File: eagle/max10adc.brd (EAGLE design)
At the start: 98 x 62 mm, 162 parts, among them IC1 MAX19506, IC2 MAX19506, J1 MOLEX_BNC_73100-0105, J2 MOLEX_BNC_73100-0105, J3 MOLEX_BNC_73100-0105, J4 MOLEX_BNC_73100-0105, K1 AQY21SOP, K2 AQY21SOP, K3 AQY21SOP, K4 AQY21SOP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

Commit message: 8.6 improvements
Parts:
- removed PIN_ANALOG, PIN_EXP_IO_1, PIN_EXP_IO_2, PIN_IO_2, PIN_PWRGND_AIN: MF-CON-2.54mm-01x08, Seeed-Connector -2016:H8-2.54
- added K5, K6, K7, K8: AQY21SOP, relay:SOP04
- added LED6, LED7, LED8: MF-LED-0805-RED, led:SML0805
- added PIN_AIN_IO2_PWRGND, PIN_ANALOG_IOEXP: 15-91-2160, pinhead+:2X08_SMT
- added RIN1_10K, RIN2_10K, RIN3_10K, RIN4_10K: 10K, resistor:R0805
- added RLED6, RLED7, RLED8: 560, resistor:R0805
- moved LED5 55.6 mm to (7.80, 1.00)
- moved RLED5 48.0 mm to (4.50, -0.40)
- moved R_SDA 20.2 mm to (-2.60, 23.6)
- moved R_SCL 19.9 mm to (2.90, 23.6)
- moved IOEXPAND_0X20_BOT 19.1 mm to (1.20, 30.5)
- moved RS9 8.00 mm to (-8.48, 3.03)
- moved IOEXPAND_0X24_TOP 1.41 mm to (12.0, 12.5)
- moved C-AIN1 1.00 mm to (57.1, 17.7)
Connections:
- removed net E_20_A6: IOEXPAND_0X20_BOT.27, PIN_EXP_IO_1.1
- removed net E_20_A7: IOEXPAND_0X20_BOT.28, PIN_EXP_IO_1.2
- removed net E_20_B5: IOEXPAND_0X20_BOT.6, PIN_EXP_IO_1.3
- removed net E_20_B6: IOEXPAND_0X20_BOT.7, PIN_EXP_IO_1.4
- removed net E_24_A5: IOEXPAND_0X24_TOP.26, PIN_EXP_IO_1.6
- removed net E_24_A6: IOEXPAND_0X24_TOP.27, PIN_EXP_IO_1.7
- removed net E_24_A7: IOEXPAND_0X24_TOP.28, PIN_EXP_IO_1.8
- new net E_HIGHGAIN1: IOEXPAND_0X20_BOT.25, K5.1
- new net E_HIGHGAIN2: IOEXPAND_0X20_BOT.26, K6.1
- new net E_HIGHGAIN3: IOEXPAND_0X20_BOT.27, K7.1
- new net E_HIGHGAIN4: IOEXPAND_0X20_BOT.28, K8.1
- new net LED6: IOEXPAND_0X24_TOP.26, LED6.A
- new net LED7: IOEXPAND_0X24_TOP.27, LED7.A
- new net LED8: IOEXPAND_0X24_TOP.28, LED8.A
- new net N$20: K5.4, RIN1_10K.1
- new net N$22: LED8.C, RLED8.1
- new net N$38: K6.4, RIN2_10K.1
- new net N$39: CIN3.1, C_AC3.1, K3.4, K7.3, RIN3.1
- new net N$40: K7.4, RIN3_10K.1
- new net N$41: CIN4.1, C_AC4.1, K4.4, K8.3, RIN4.1
- new net N$42: K8.4, RIN4_10K.1
- net +3V3: now also PIN_AIN_IO2_PWRGND.14, PIN_AIN_IO2_PWRGND.16; no longer PIN_PWRGND_AIN.1, PIN_PWRGND_AIN.2
- net +5V: now also PIN_AIN_IO2_PWRGND.10, PIN_AIN_IO2_PWRGND.12; no longer PIN_PWRGND_AIN.3, PIN_PWRGND_AIN.4
- net A10: now also PIN_ANALOG_IOEXP.8; no longer PIN_ANALOG.5
- net A11: now also PIN_ANALOG_IOEXP.10; no longer PIN_ANALOG.4
- net A12: now also PIN_ANALOG_IOEXP.12; no longer PIN_ANALOG.3
- net A13: now also PIN_ANALOG_IOEXP.14; no longer PIN_ANALOG.2
- net A14: now also PIN_ANALOG_IOEXP.16; no longer PIN_ANALOG.1
- net A6: now also PIN_ANALOG_IOEXP.2; no longer PIN_ANALOG.8
- net A7: now also PIN_ANALOG_IOEXP.4; no longer PIN_ANALOG.7
- net A8: now also PIN_ANALOG_IOEXP.6; no longer PIN_ANALOG.6
- net AIN1: now also PIN_AIN_IO2_PWRGND.1; no longer PIN_PWRGND_AIN.5
- net E_20_B7: now also PIN_AIN_IO2_PWRGND.2; no longer PIN_EXP_IO_1.5
- net E_24_B0: now also PIN_ANALOG_IOEXP.1; no longer PIN_EXP_IO_2.1
- net E_24_B1: now also PIN_ANALOG_IOEXP.3; no longer PIN_EXP_IO_2.2
- net E_24_B2: now also PIN_ANALOG_IOEXP.5; no longer PIN_EXP_IO_2.3
- net E_24_B3: now also PIN_ANALOG_IOEXP.7; no longer PIN_EXP_IO_2.4
- net E_24_B4: now also PIN_ANALOG_IOEXP.9; no longer PIN_EXP_IO_2.5
- net E_24_B5: now also PIN_ANALOG_IOEXP.11; no longer PIN_EXP_IO_2.6
- net E_24_B6: now also PIN_ANALOG_IOEXP.13; no longer PIN_EXP_IO_2.7
- net E_24_B7: now also PIN_ANALOG_IOEXP.15; no longer PIN_EXP_IO_2.8
- net E_OVSAMP1: now also IOEXPAND_0X20_BOT.6; no longer IOEXPAND_0X20_BOT.25
- net E_OVSAMP2: now also IOEXPAND_0X20_BOT.7; no longer IOEXPAND_0X20_BOT.26
- net GND: now also K5.2, K6.2, K7.2, K8.2, PIN_AIN_IO2_PWRGND.4, PIN_AIN_IO2_PWRGND.6, PIN_AIN_IO2_PWRGND.8, RLED6.2, RLED7.2, RLED8.2; no longer PIN_IO_2.1, PIN_PWRGND_AIN.6, PIN_PWRGND_AIN.7, PIN_PWRGND_AIN.8
- net INAMINUS1: now also RIN1_10K.2
- net INAMINUS2: now also RIN3_10K.2
- net INBMINUS1: now also RIN2_10K.2
- net INBMINUS2: now also RIN4_10K.2
- net IO_100: now also PIN_AIN_IO2_PWRGND.11; no longer PIN_IO_2.6
- net IO_101: now also PIN_AIN_IO2_PWRGND.13; no longer PIN_IO_2.7
- net IO_CLK_88: now also PIN_AIN_IO2_PWRGND.3; no longer PIN_IO_2.2
- net IO_CLK_89: now also PIN_AIN_IO2_PWRGND.5; no longer PIN_IO_2.3
- net IO_CLK_90: now also PIN_AIN_IO2_PWRGND.7; no longer PIN_IO_2.4
- net IO_CLK_91: now also PIN_AIN_IO2_PWRGND.9; no longer PIN_IO_2.5
- net L121: now also PIN_AIN_IO2_PWRGND.15; no longer PIN_IO_2.8
- net N$10: now also K5.3
- net N$15: now also K6.3
- net N$16: now also LED6.C, RLED6.1; no longer CIN3.1, C_AC3.1, K3.4, RIN3.1
- net N$19: now also LED7.C, RLED7.1; no longer CIN4.1, C_AC4.1, K4.4, RIN4.1
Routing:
- net E_HIGHGAIN2: track 0.00 -> 96.9 mm, vias 0 -> 2
- net E_HIGHGAIN4: track 0.00 -> 84.6 mm, vias 0 -> 2
- net E_HIGHGAIN3: track 0.00 -> 76.3 mm, vias 0 -> 6
- net +3V3: track 484.0 -> 557.8 mm
- net E_HIGHGAIN1: track 0.00 -> 72.7 mm, vias 0 -> 2
- net +5V: track 281.1 -> 345.7 mm
- net LED5: track 72.3 -> 9.53 mm, vias 2 -> 0
- net E_20_A6: track 47.5 -> 0.00 mm, vias 2 -> 0
- net E_ACSW4: track 148.2 -> 102.3 mm, vias 2 -> 3
- net E_20_A7: track 44.3 -> 0.00 mm, vias 2 -> 0
- net E_20_B6: track 40.5 -> 0.00 mm, vias 3 -> 0
- net SERIALTOLEFT_96: track 86.3 -> 47.5 mm, vias 3 -> 1
- net E_20_B5: track 34.7 -> 0.00 mm, vias 2 -> 0
- net N$41: track 0.00 -> 29.1 mm, vias 0 -> 1
- net E_GSW4: track 119.6 -> 90.6 mm
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
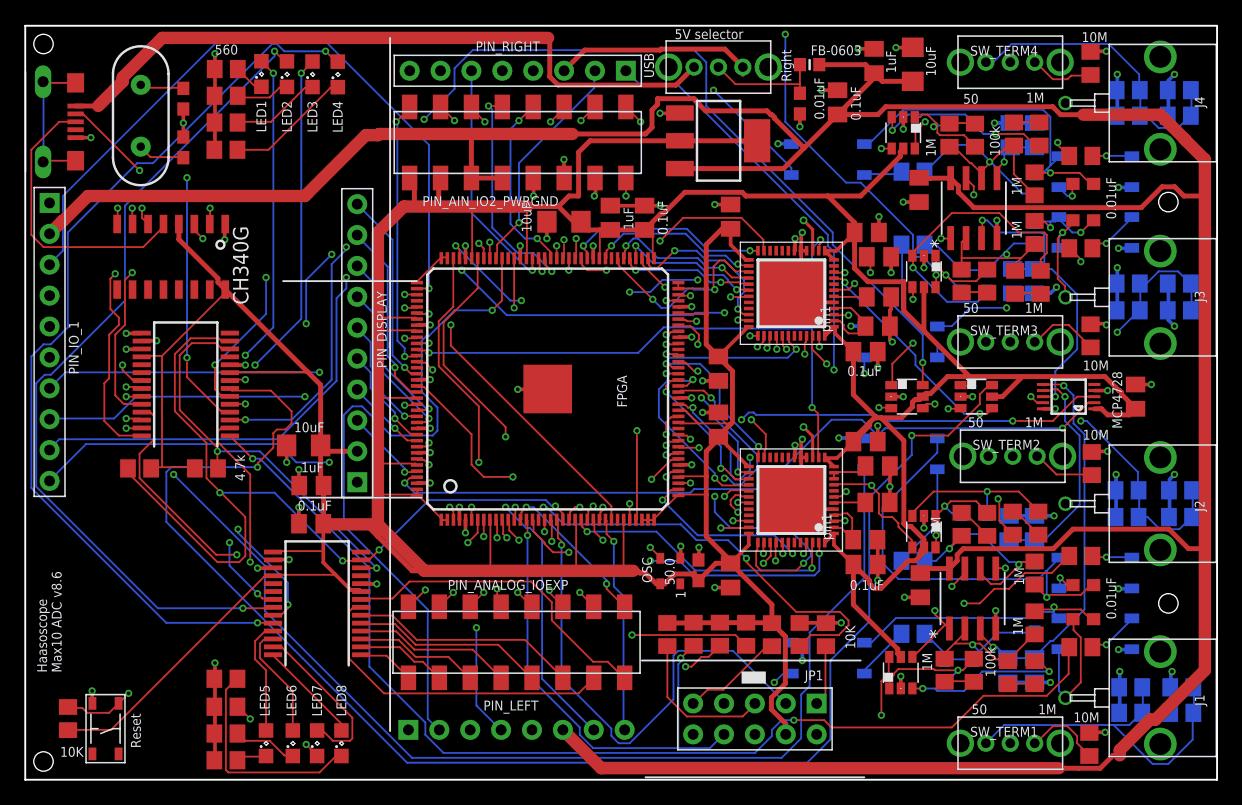
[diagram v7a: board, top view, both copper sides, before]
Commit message: updates for v8.5 and v8.6
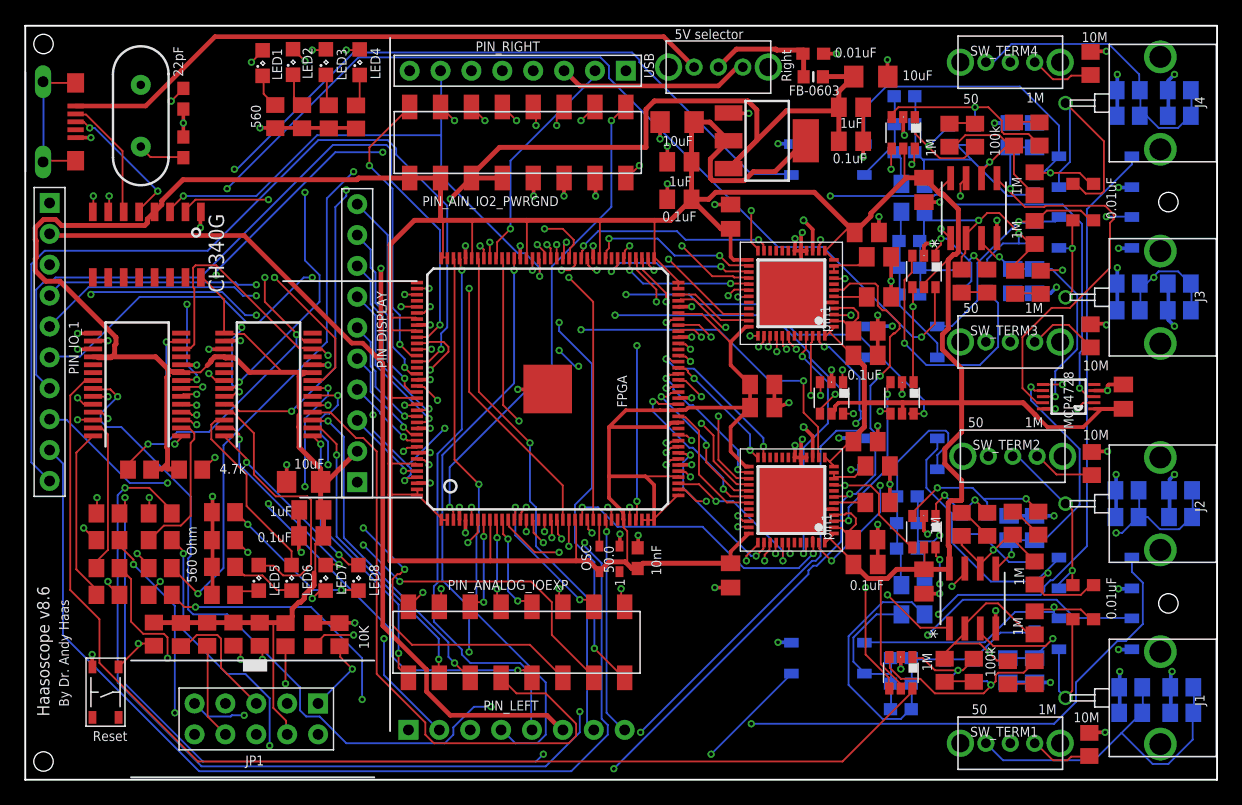
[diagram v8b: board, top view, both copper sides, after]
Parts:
- added CIN1NF_1, CIN1NF_2, CIN1NF_3, CIN1NF_4: 1nF, rcl@1:C0603
- added CIN56_1, CIN56_2, CIN56_3, CIN56_4, CIN56_5, CIN56_6, CIN56_7, CIN56_8: 56pF, rcl@1:C0603
- added HGR1, HGR2, HGR3, HGR4: 560, resistor:R0805
- moved ACR4 83.9 mm to (-0.90, 13.2)
- moved ACR3 80.1 mm to (-0.90, 15.4)
- moved ACR1 76.5 mm to (-0.90, 19.9)
- moved ACR2 75.7 mm to (-0.90, 17.7)
- moved JP1 41.0 mm to (7.00, 3.00)
- moved RJ2 40.0 mm to (13.8, 9.93)
- moved RJ3 40.0 mm to (0.80, 9.94)
- moved RJ4 40.0 mm to (9.40, 9.93)
- moved RJ5 40.0 mm to (2.96, 9.96)
- moved RS6 40.0 mm to (11.7, 9.94)
- moved RS7 40.0 mm to (5.12, 9.97)
- moved RS8 40.0 mm to (7.28, 9.96)
- moved IOEXPAND_0X24_TOP 18.4 mm to (8.00, 30.5)
- moved RLED6 13.7 mm to (4.30, 15.5)
- moved RLED7 13.7 mm to (4.30, 17.7)
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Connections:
- new net N$34: HGR1.2, K5.1
- new net N$36: HGR2.2, K6.1
- new net N$37: HGR3.2, K7.1
- new net N$43: HGR4.2, K8.1
- net +3V3: now also C5VOPAMP1.1, C5VOPAMP2.1, U1.8, U2.8
- net +5V: no longer C5VOPAMP1.1, C5VOPAMP2.1, U1.8, U2.8
- net E_HIGHGAIN1: now also HGR1.1; no longer K5.1
- net E_HIGHGAIN2: now also HGR2.1; no longer K6.1
- net E_HIGHGAIN3: now also HGR3.1; no longer K7.1
- net E_HIGHGAIN4: now also HGR4.1; no longer K8.1
- net INAMINUS1: now also CIN1NF_1.2, CIN56_1.2, CIN56_2.2
- net INAMINUS2: now also CIN1NF_3.2, CIN56_5.2, CIN56_6.2
- net INBMINUS1: now also CIN1NF_2.2, CIN56_3.2, CIN56_4.2
- net INBMINUS2: now also CIN1NF_4.2, CIN56_7.2, CIN56_8.2
- net N$20: now also CIN1NF_1.1, CIN56_1.1, CIN56_2.1
- net N$38: now also CIN1NF_2.1, CIN56_3.1, CIN56_4.1
- net N$40: now also CIN1NF_3.1, CIN56_5.1, CIN56_6.1
- net N$42: now also CIN1NF_4.1, CIN56_7.1, CIN56_8.1
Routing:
- net +5V: track 345.7 -> 148.2 mm, vias 0 -> 2
- net N$35: track 3.28 -> 122.7 mm, vias 1 -> 3
- net N$32: track 4.36 -> 118.3 mm, vias 1 -> 3
- net N$11: track 4.27 -> 114.7 mm, vias 1 -> 3
- net N$36: track 0.00 -> 105.9 mm, vias 0 -> 3
- net N$21: track 3.32 -> 104.2 mm, vias 1 -> 3
- net N$37: track 0.00 -> 94.5 mm, vias 0 -> 2
- net N$43: track 0.00 -> 93.8 mm, vias 0 -> 2
- net E_ACSW3: track 102.6 -> 16.3 mm, vias 3 -> 2
- net E_HIGHGAIN2: track 96.9 -> 11.9 mm
- net E_ACSW4: track 102.3 -> 18.3 mm, vias 3 -> 2
- net E_ACSW1: track 90.8 -> 7.57 mm
- net E_ACSW2: track 94.3 -> 12.4 mm, vias 2 -> 0
- net N$34: track 0.00 -> 77.3 mm, vias 0 -> 3
- net E_HIGHGAIN4: track 84.6 -> 14.4 mm, vias 2 -> 0
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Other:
- board text added: "0.1uF"
- board text added: "10k"
- board text added: "10nF"
- board text added: "1nF+56pFx2"
- board text added: "1uF"
- board text added: "22pF"
- board text added: "560 Ohm"
- board text added: "By Dr. Andy Haas"
- board text added: "Haasoscope v8.6"
- board text removed: "10K"
- board text removed: "Haasoscope"
- board text removed: "Max10 ADC v8.6"
